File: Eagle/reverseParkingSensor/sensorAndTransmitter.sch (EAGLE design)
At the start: 29 parts, among them IC1 LM393N, IC3 MEGA8-P, Q1 BC558B, T1 BPX81, X1 YH-55-10

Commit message: final pcb for sensor and transmitter
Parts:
- added LED1: (no value), led:LED3MM
- added R6: 220, resistor:R-EU_0207/10
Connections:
- new net N$6: IC3.PB1(OC1A), R6.1
- new net N$7: LED1.A, R6.2
- net GND: now also LED1.C
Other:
- moved on the sheet: X1
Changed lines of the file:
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@@
 <part name="P+1" library="supply1" deviceset="+5V" device=""/>
 <part name="Q1" library="transistor-pnp" deviceset="BC558*" device="" technology="B"/>
+<part name="LED1" library="led" deviceset="LED" device="3MM"/>
+<part name="R6" library="resistor" deviceset="R-EU_" device="0207/10" value="220"/>
+<part name="GND1" library="supply1" deviceset="GND" device=""/>
 </parts>
 <sheets>
@@
 <instance part="JP4" gate="1" x="190.5" y="86.36" rot="R270"/>
 <instance part="JP5" gate="1" x="190.5" y="63.5" rot="R90"/>
-<instance part="GND18" gate="1" x="264.16" y="50.8" rot="R90"/>
-<instance part="X1" gate="G$1" x="256.54" y="48.26"/>
-<instance part="P+1" gate="1" x="261.62" y="45.72" rot="R270"/>
+<instance part="GND18" gate="1" x="213.36" y="30.48" rot="R270"/>
+<instance part="X1" gate="G$1" x="241.3" y="27.94"/>
+<instance part="P+1" gate="1" x="218.44" y="25.4" rot="R90"/>
 <instance part="Q1" gate="G$1" x="-30.48" y="35.56" rot="R180"/>
+<instance part="LED1" gate="G$1" x="236.22" y="45.72" rot="R90"/>
+<instance part="R6" gate="G$1" x="226.06" y="45.72"/>
+<instance part="GND1" gate="1" x="246.38" y="45.72" rot="R90"/>
 </instances>
 <busses>
@@
 <pinref part="P+1" gate="1" pin="+5V"/>
 <pinref part="X1" gate="G$1" pin="5"/>
-<wire x1="259.08" y1="45.72" x2="248.92" y2="45.72" width="0.1524" layer="91"/>
+<wire x1="220.98" y1="25.4" x2="233.68" y2="25.4" width="0.1524" layer="91"/>
 </segment>
 </net>
@@
 <pinref part="GND18" gate="1" pin="GND"/>
 <pinref part="X1" gate="G$1" pin="3"/>
-<wire x1="261.62" y1="50.8" x2="248.92" y2="50.8" width="0.1524" layer="91"/>
+<wire x1="215.9" y1="30.48" x2="233.68" y2="30.48" width="0.1524" layer="91"/>
+</segment>
+<segment>
+<pinref part="GND1" gate="1" pin="GND"/>
+<pinref part="LED1" gate="G$1" pin="C"/>
+<wire x1="243.84" y1="45.72" x2="241.3" y2="45.72" width="0.1524" layer="91"/>
 </segment>
 </net>
@@
 <segment>
 <pinref part="IC3" gate="G$1" pin="PB0(ICP)"/>
-<wire x1="215.9" y1="48.26" x2="220.98" y2="50.8" width="0.1524" layer="91"/>
-<label x="220.98" y="50.8" size="1.778" layer="95" xref="yes"/>
+<wire x1="215.9" y1="48.26" x2="220.98" y2="53.34" width="0.1524" layer="91"/>
+<label x="220.98" y="53.34" size="1.778" layer="95" xref="yes"/>
 </segment>
 </net>
@@
 <wire x1="215.9" y1="40.64" x2="187.96" y2="40.64" width="0.1524" layer="91"/>
 <pinref part="X1" gate="G$1" pin="2"/>
-<wire x1="215.9" y1="40.64" x2="248.92" y2="53.34" width="0.1524" layer="91"/>
+<wire x1="215.9" y1="40.64" x2="233.68" y2="33.02" width="0.1524" layer="91"/>
 </segment>
 </net>
@@
 <wire x1="215.9" y1="35.56" x2="187.96" y2="35.56" width="0.1524" layer="91"/>
 <pinref part="X1" gate="G$1" pin="6"/>
-<wire x1="215.9" y1="35.56" x2="248.92" y2="43.18" width="0.1524" layer="91"/>
+<wire x1="215.9" y1="35.56" x2="233.68" y2="22.86" width="0.1524" layer="91"/>
 </segment>
 </net>
@@
 <wire x1="215.9" y1="38.1" x2="187.96" y2="38.1" width="0.1524" layer="91"/>
 <pinref part="X1" gate="G$1" pin="4"/>
-<wire x1="215.9" y1="38.1" x2="248.92" y2="48.26" width="0.1524" layer="91"/>
+<wire x1="215.9" y1="38.1" x2="233.68" y2="27.94" width="0.1524" layer="91"/>
 </segment>
 </net>
@@
 <pinref part="IC3" gate="G$1" pin="PB2(SS/OC1B)"/>
 <pinref part="X1" gate="G$1" pin="1"/>
-<wire x1="215.9" y1="43.18" x2="248.92" y2="55.88" width="0.1524" layer="91"/>
-</segment>
-</net>
+<wire x1="215.9" y1="43.18" x2="233.68" y2="35.56" width="0.1524" layer="91"/>
+</segment>
+</net>
+<net name="N$6" class="0">
+<segment>
+<pinref part="IC3" gate="G$1" pin="PB1(OC1A)"/>
+<pinref part="R6" gate="G$1" pin="1"/>
+<wire x1="220.98" y1="45.72" x2="215.9" y2="45.72" width="0.1524" layer="91"/>
+</segment>
+</net>
+<net name="N$7" class="0">
+<segment>
+<pinref part="R6" gate="G$1" pin="2"/>
+<pinref part="LED1" gate="G$1" pin="A"/>
+<wire x1="231.14" y1="45.72" x2="233.68" y2="45.72" width="0.1524" layer="91"/>
+</segment>
+</net>

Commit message: final pcb
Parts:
- added JP1: (no value), jumper:JP1E
- R4: device resistor:R-EU_0204/2V -> resistor:R-EU_0204/5
- R6: device resistor:R-EU_0207/10 -> resistor:R-EU_0204/2V
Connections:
- new net N$8: IC3.PB1(OC1A), X1.4
- new net N$9: IC3.PB2(SS/OC1B), X1.2
- net +5V: now also JP1.2; no longer X1.5
- net GND: now also JP1.1, R6.2; no longer LED1.C, X1.3
- net N$5: now also IC3.PB0(ICP); no longer IC3.PB2(SS/OC1B)
- net N$6: now also LED1.C; no longer IC3.PB1(OC1A)
- net N$7: now also IC3.PD7(AIN1); no longer R6.2
- net PB3: now also X1.6; no longer X1.2
- net PB4: now also X1.5; no longer X1.4
- net PB5: now also X1.3; no longer X1.6
- net UPHOLD: now also IC3.PD6(AIN0); no longer IC3.PB0(ICP)
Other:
- moved on the sheet: LED1, R6

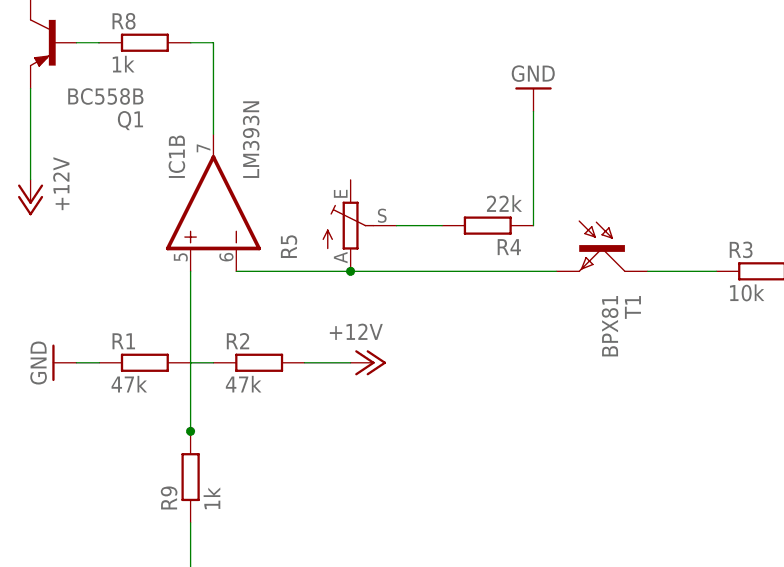
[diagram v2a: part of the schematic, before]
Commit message: sime test only sending increasing integers and displays is
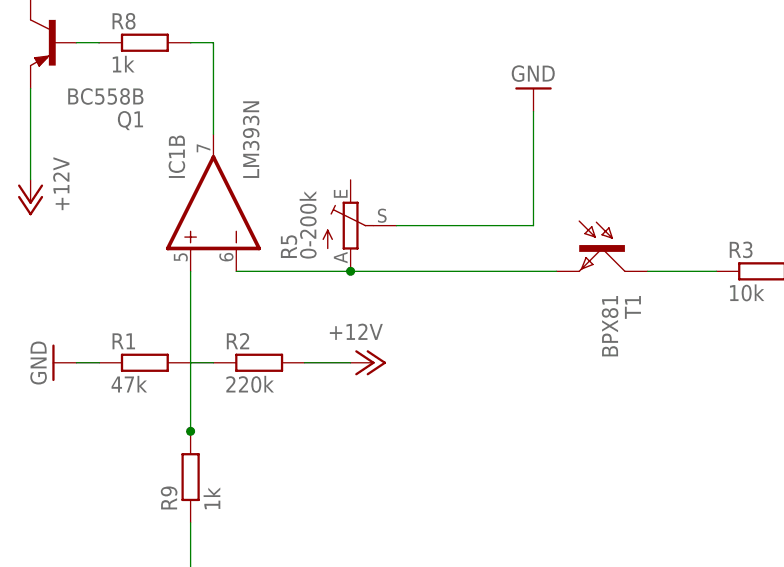
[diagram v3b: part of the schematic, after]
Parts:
- removed R4: 22k, resistor:R-EU_0204/5
- R2: value 47k -> 220k
- R5: value (none) -> 0-200k
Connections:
- removed net N$4: R4.2, R5.S
- net GND: now also R5.S; no longer R4.1
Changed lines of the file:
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@@
 <part name="IC1" library="linear" deviceset="LM393" device="N"/>
 <part name="R1" library="resistor" deviceset="R-EU_" device="0204/5" value="47k"/>
-<part name="R2" library="resistor" deviceset="R-EU_" device="0204/2V" value="47k"/>
+<part name="R2" library="resistor" deviceset="R-EU_" device="0204/2V" value="220k"/>
 <part name="T1" library="opto-trans-siemens" deviceset="BPX81" device=""/>
 <part name="R3" library="resistor" deviceset="R-EU_" device="0204/5" value="10k"/>
-<part name="R4" library="resistor" deviceset="R-EU_" device="0204/5" value="22k"/>
-<part name="R5" library="pot" deviceset="TRIM_EU-" device="CA6V"/>
+<part name="R5" library="pot" deviceset="TRIM_EU-" device="CA6V" value="0-200k"/>
 <part name="IC10" library="v-reg" deviceset="78XXL" device=""/>
 <part name="P+20" library="supply1" deviceset="+5V" device=""/>
@@
 <instance part="T1" gate="1" x="30.48" y="12.7" rot="R270"/>
 <instance part="R3" gate="G$1" x="48.26" y="10.16"/>
-<instance part="R4" gate="G$1" x="17.78" y="15.24" rot="R180"/>
 <instance part="R5" gate="1" x="2.54" y="15.24"/>
 <instance part="IC10" gate="A" x="139.7" y="-17.78"/>
@@
 </segment>
 <segment>
-<pinref part="R4" gate="G$1" pin="1"/>
 <wire x1="22.86" y1="15.24" x2="22.86" y2="27.94" width="0.1524" layer="91"/>
 <pinref part="GND23" gate="1" pin="GND"/>
+<pinref part="R5" gate="1" pin="S"/>
+<wire x1="22.86" y1="15.24" x2="7.62" y2="15.24" width="0.1524" layer="91"/>
 </segment>
 <segment>
@@
 </segment>
 </net>
-<net name="N$4" class="0">
-<segment>
-<pinref part="R4" gate="G$1" pin="2"/>
-<pinref part="R5" gate="1" pin="S"/>
-<wire x1="12.7" y1="15.24" x2="7.62" y2="15.24" width="0.1524" layer="91"/>
-</segment>
-</net>
